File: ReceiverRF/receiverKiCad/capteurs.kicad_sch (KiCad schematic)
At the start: 10 parts, among them J1 Conn_Coaxial, J3 Conn_01x04, U4 MLX90393SLW-ABA-011-RE

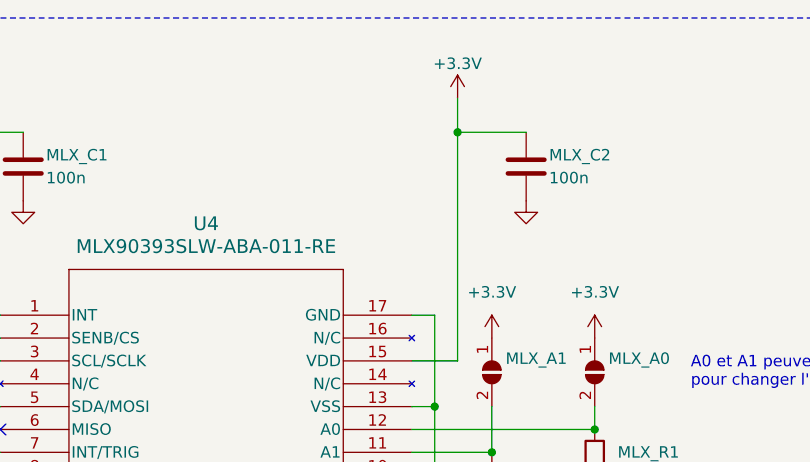
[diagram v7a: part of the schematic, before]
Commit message: Début PCB. Groupement et placement des composantes.
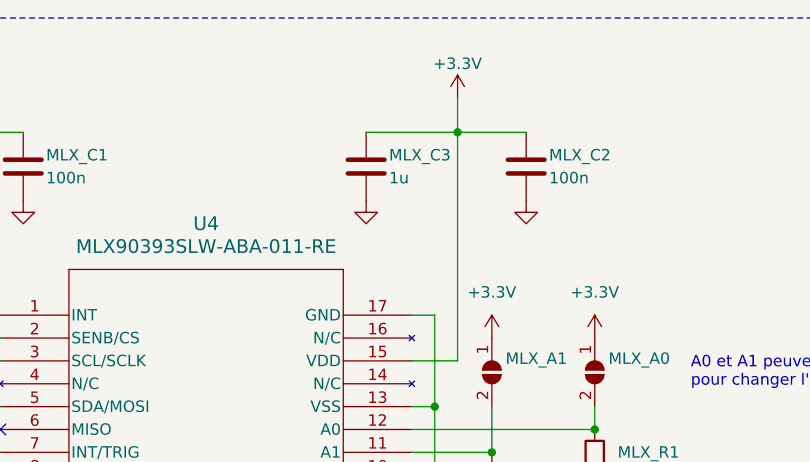
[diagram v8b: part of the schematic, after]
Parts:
- added MLX_C3: 1u, Capacitor_SMD:C_0603_1608Metric, symbol Device:C
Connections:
- net +3.3V: now also MLX_C3.1
- net GND: now also MLX_C3.2
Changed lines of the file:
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@@
+	(wire
+		(pts
+			(xy 85.09 31.75) (xy 95.25 31.75)
+		)
+		(stroke
+			(width 0)
+			(type default)
+		)
+	)
 	(wire
 		(pts
@@
 	)
 	(symbol
+		(lib_id "power:GND")
+		(at 85.09 39.37 0)
+		(unit 1)
+		(exclude_from_sim no)
+		(in_bom yes)
+		(on_board yes)
+		(dnp no)
+		(fields_autoplaced yes)
+		(property "Reference" "#PWR063"
+			(at 85.09 45.72 0)
+			(effects
+				(font
+					(size 1.27 1.27)
+				)
+				(hide yes)
+			)
+		)
+		(property "Value" "GND"
+			(at 85.09 44.45 0)
+			(effects
+				(font
+					(size 1.27 1.27)
+				)
+				(hide yes)
+			)
+		)
+		(property "Footprint" ""
+			(at 85.09 39.37 0)
+			(effects
+				(font
+					(size 1.27 1.27)
+				)
+				(hide yes)
+			)
+		)
+		(property "Datasheet" ""
+			(at 85.09 39.37 0)
+			(effects
+				(font
+					(size 1.27 1.27)
+				)
+				(hide yes)
+			)
+		)
+		(property "Description" ""
+			(at 85.09 39.37 0)
+			(effects
+				(font
+					(size 1.27 1.27)
+				)
+				(hide yes)
+			)
+		)
+		(pin "1"
+		)
+		(instances
+			(project "receiver"
+				(path "/439ba515-58d4-4b14-87ab-b438dcf423a5/56b56711-4d65-4df6-9470-6736a83e438d"
+					(reference "#PWR063")
+					(unit 1)
+				)
+			)
+		)
+	)
+	(symbol
 		(lib_id "Jumper:SolderJumper_2_Open")
 		(at 110.49 58.42 270)
@@
 					(unit 1)
 				)
+			)
+		)
+	)
+	(symbol
+		(lib_id "Device:C")
+		(at 85.09 35.56 0)
+		(unit 1)
+		(exclude_from_sim no)
+		(in_bom yes)
+		(on_board yes)
+		(dnp no)
+		(property "Reference" "MLX_C3"
+			(at 87.63 34.29 0)
+			(effects
+				(font
+					(size 1.27 1.27)
+				)
+				(justify left)
+			)
+		)
+		(property "Value" "1u"
+			(at 87.63 36.83 0)
+			(effects
+				(font
+					(size 1.27 1.27)
+				)
+				(justify left)
+			)
+		)
+		(property "Footprint" "Capacitor_SMD:C_0603_1608Metric"
+			(at 86.0552 39.37 0)
+			(effects
+				(font
+					(size 1.27 1.27)
+				)
+				(hide yes)
+			)
+		)
+		(property "Datasheet" "~"
+			(at 85.09 35.56 0)
+			(effects
+				(font
+					(size 1.27 1.27)
+				)
+				(hide yes)
+			)
+		)
+		(property "Description" ""
+			(at 85.09 35.56 0)
+			(effects
+				(font
+					(size 1.27 1.27)
+				)
+				(hide yes)
+			)
+		)
+		(pin "1"
+		)
+		(pin "2"
+		)
+		(instances
+			(project "receiver"
+				(path "/439ba515-58d4-4b14-87ab-b438dcf423a5/56b56711-4d65-4df6-9470-6736a83e438d"
+					(reference "MLX_C3")
+					(unit 1)
+				)
